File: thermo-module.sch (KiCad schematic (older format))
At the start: 0 parts

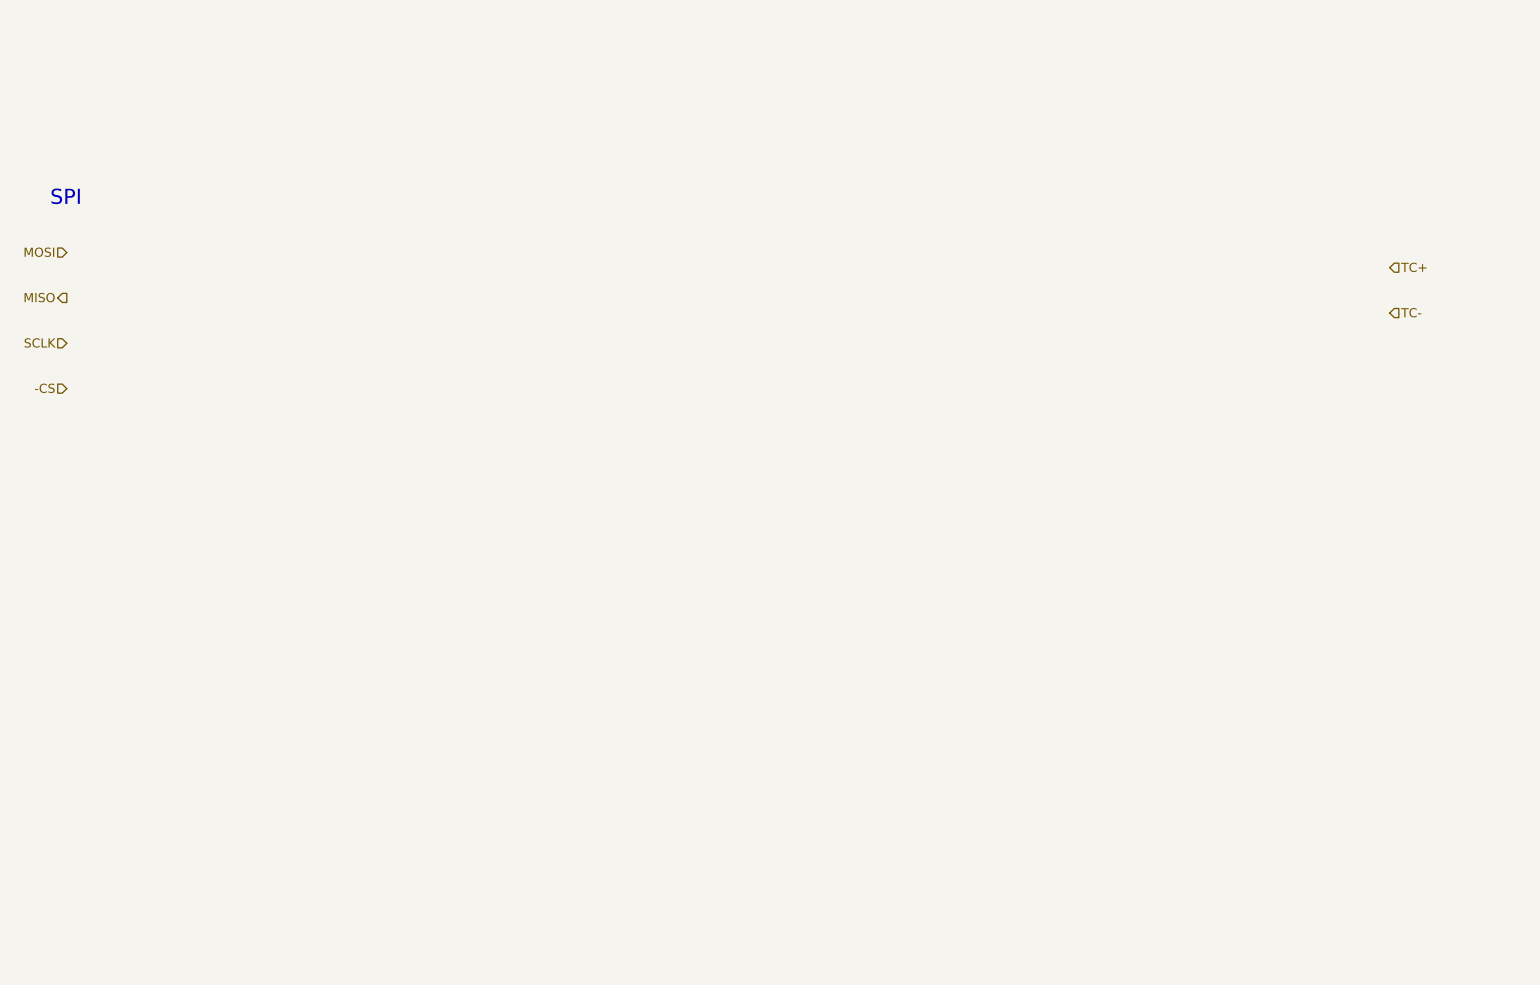
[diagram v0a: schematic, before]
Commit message: Adds thermo module circuit
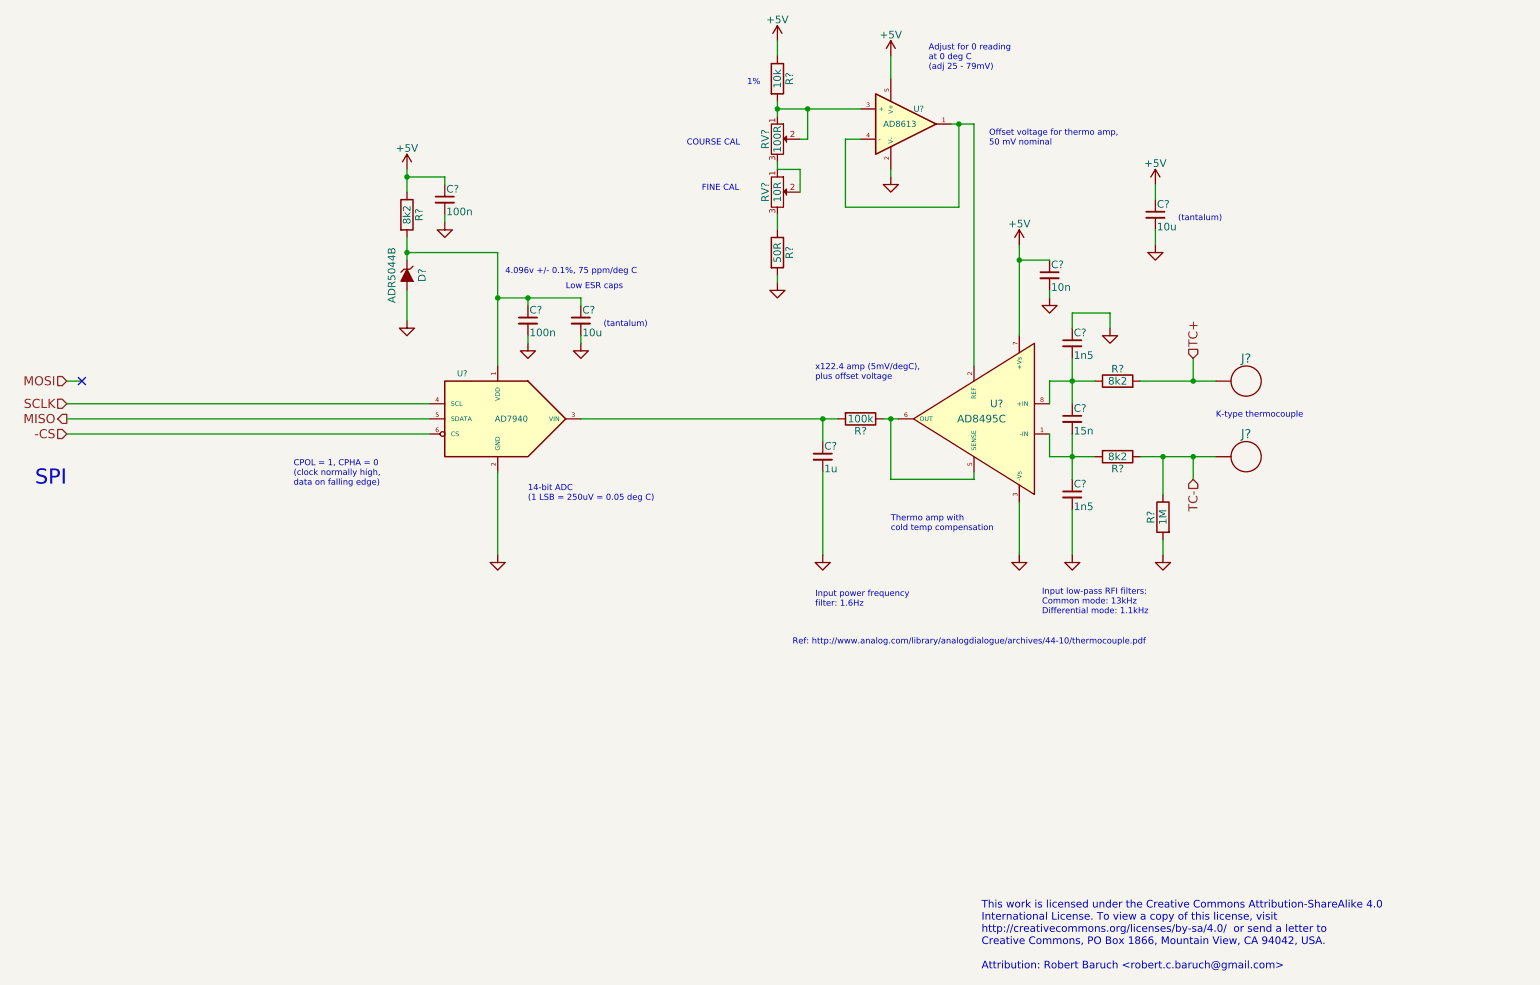
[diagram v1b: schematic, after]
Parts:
- added C?: 15n, symbol C_Small
- added C? (x2): 1n5, symbol C_Small
- added C?: 1u, symbol C_Small
- added C?: 10n, symbol C_Small
- added C? (x2): 10u, symbol C_Small
- added C? (x2): 100n, symbol C_Small
- added D?: ADR5044B, symbol ZENERsmall
- added J? (x2): BANANA, symbol BANANA
- added R?: 1M, symbol R
- added R?: 10k, symbol R
- added R? (x3): 8k2, symbol R
- added R?: 100k, symbol R
- added R?: 50R, symbol R
- added RV?: 100R, symbol POT
- added RV?: 10R, symbol POT
- added U?: AD8495C, symbol AD8495C
- added U?: AD8613, symbol AD8613
- added U?: AD7940, symbol AD7940
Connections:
- net -CS: now also U?.6 (CS)
- net MISO: now also U?.5 (SDATA)
- net SCLK: now also U?.4 (SCL)
- net TC+: now also J?.1 (X), R?.2
- net TC-: now also J?.1 (X), R?.1, R?.1
- new net: C?.1, C?.2, R?.2, U?.1 (-IN)
- new net: U?.1, U?.2 (REF), U?.4 (-)
- new net: R?.1, U?.5 (SENSE), U?.6 (OUT)
- new net: C?.1, C?.2, R?.1, U?.8 (+IN)
- new net: R?.2, RV?.1, RV?.2, U?.3 (+)
- new net: RV?.1, RV?.2, RV?.3
- new net: C?.1, R?.2, U?.3 (VIN)
- new net: C?.1, C?.1, D?.1 (K), R?.2, U?.1 (VDD)
- new net: R?.1, RV?.3
- new net +5V: C?.1, C?.1, C?.1, R?.1, R?.1, U?.5 (V+), U?.7 (+Vs)
- new net GNDA: C?.1, C?.2, C?.2, C?.2, C?.2, C?.2, C?.2, C?.2, D?.2 (A), R?.2, R?.2, U?.2 (GND), U?.2 (V-), U?.3 (-Vs)
- no-connect marks 0 -> 1
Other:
- note added: "(tantalum)"
- note added: "1%"
- note added: "14-bit ADC\n(1 LSB = 250uV = 0.05 deg C)"
- note added: "4.096v +/- 0.1%, 75 ppm/deg C"
- note added: "Adjust for 0 reading\nat 0 deg C\n(adj 25 - 79mV)"
- note added: "COURSE CAL"
- note added: "CPOL = 1, CPHA = 0\n(clock normally high,\ndata on falling edge)"
- note added: "FINE CAL"
- note added: "Input low-pass RFI filters:\nCommon mode: 13kHz\nDifferential mode: 1.1kHz"
- note added: "Input power frequency\nfilter: 1.6Hz"
- note added: "K-type thermocouple"
- note added: "Low ESR caps"
- note added: "Offset voltage for thermo amp,\n50 mV nominal"
- note added: "Ref: http://www.analog.com/library/analogdialogue/archives/44-10/thermocouple.pdf"
- note added: "Thermo amp with\ncold temp compensation"
- note added: "This work is licensed under the Creative Commons Attribution-ShareAlike 4.0 \nInternational License. To view a copy of this license, visit \nhttp://creativecommons.org/licenses/by-sa/4.0/ or send a letter to \nCreative Commons, PO Box 1866, Mountain View, CA 94042, USA.\n\nAttribution: Robert Baruch <robert.c.baruch@gmail.com>"
- note added: "x122.4 amp (5mV/degC),\nplus offset voltage"
